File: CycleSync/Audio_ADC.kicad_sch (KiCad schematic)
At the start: 21 parts, among them U6 PCM1862DBT

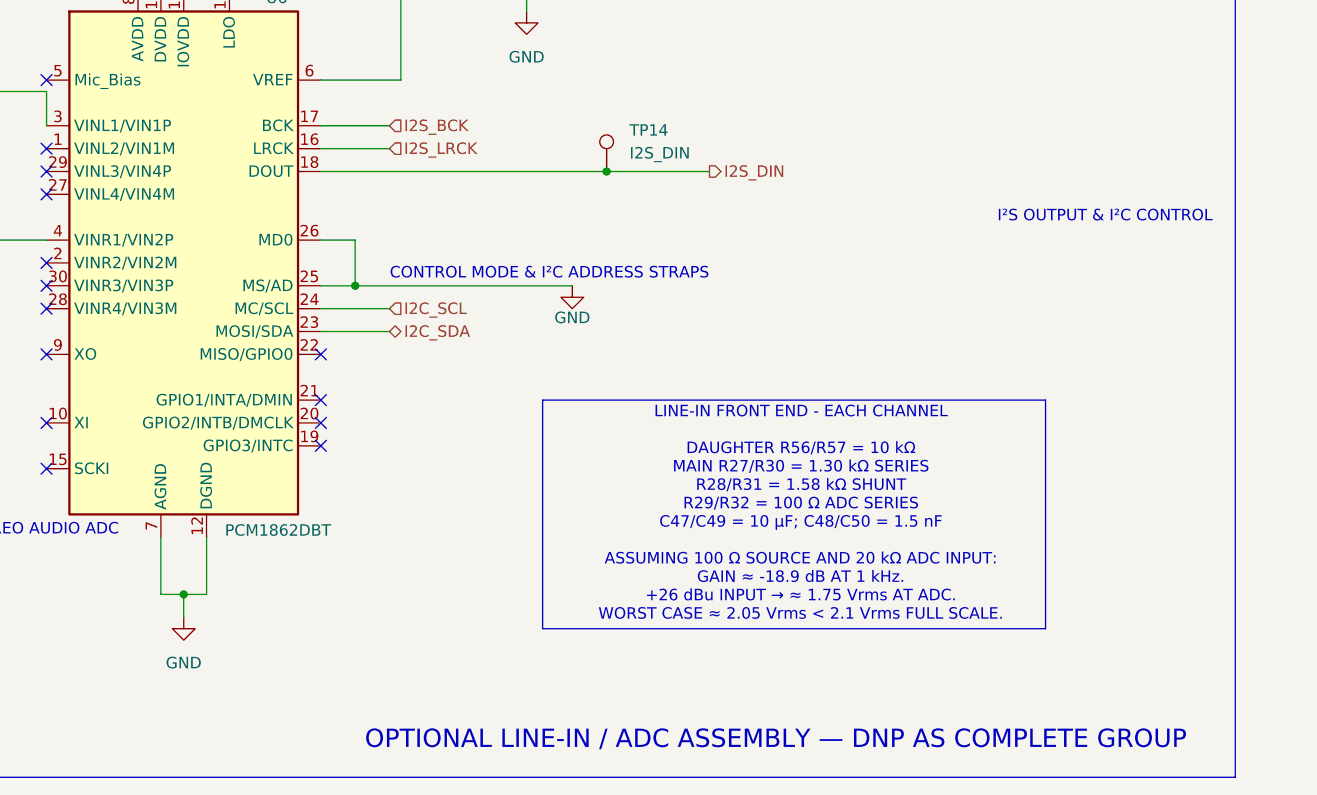
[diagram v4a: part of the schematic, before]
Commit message: added footprints and manufacturer part number
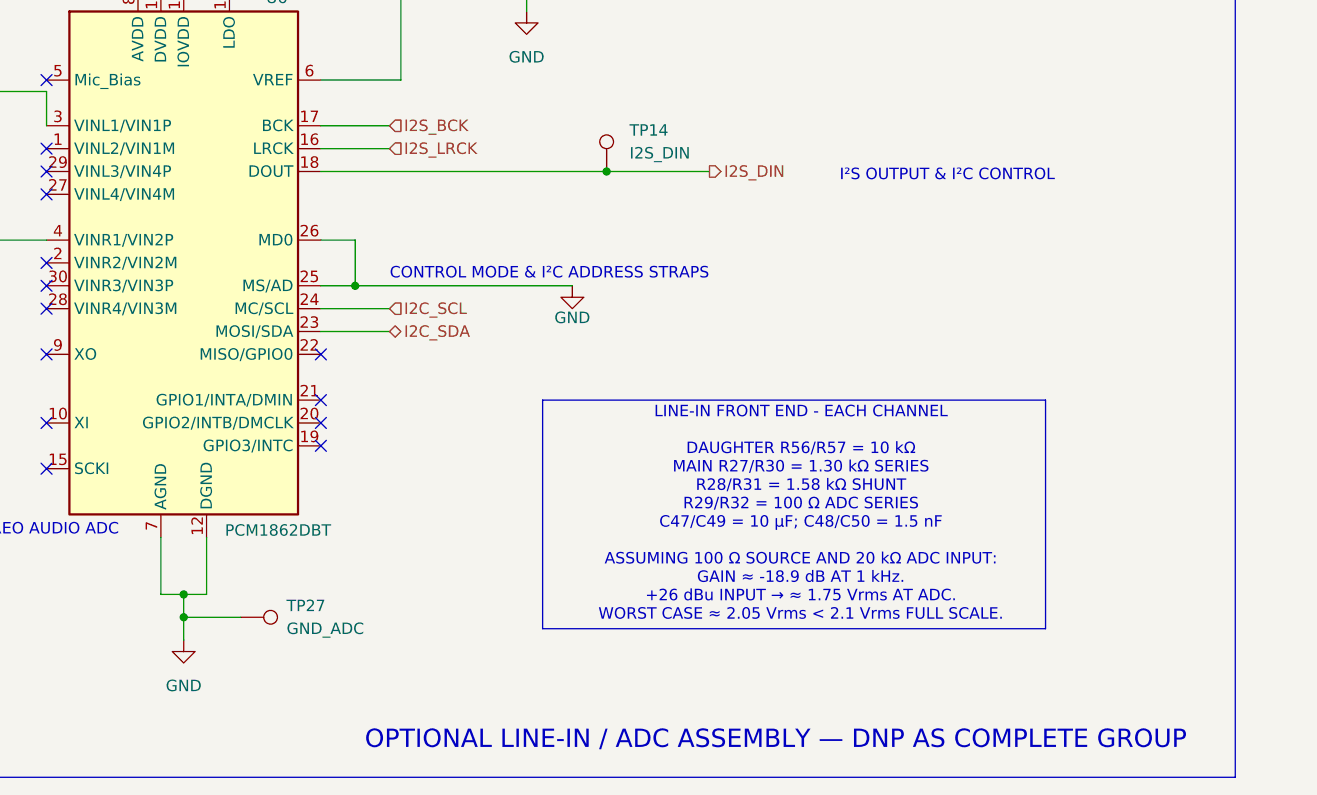
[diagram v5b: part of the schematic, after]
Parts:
- added TP27: GND_ADC, TestPoint:TestPoint_Pad_D1.5mm, symbol Connector:TestPoint
- C40, C42, C45: Distributor Link (none) -> https://jlcpcb.com/partdetail/MurataElectronics-GRM155R71A1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; MANUFACTURER (none) -> Murata Electronics; MPN (none) -> GRM155R71A104KA01D
- C41, C43, C46, C47, C49: Distributor Link (none) -> https://jlcpcb.com/partdetail/236937-GRM21BZ71E106KE15L/C23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; MANUFACTURER (none) -> Murata Electronics; MPN (none) -> GRM21BZ71E106KE15L
- C44: Distributor Link (none) -> https://jlcpcb.com/partdetail/30690-CL10B105KA8NNNC/C29936; MANUFACTURER (none) -> Samsung Electro-Mechanics; MPN (none) -> CL10B105KA8NNNC
- C48, C50: Distributor Link (none) -> https://jlcpcb.com/partdetail/173585-GRM1885C1H152JA01D/C16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; MANUFACTURER (none) -> Murata Electronics; MPN (none) -> GRM1885C1H152JA01D
- D4, D5: Distributor Link (none) -> https://jlcpcb.com/partdetail/Nexperia-PESD24VL1BA115/C69324; MANUFACTURER (none) -> Nexperia; MPN (none) -> PESD24VL1BA,115
- R27, R30: Distributor Link (none) -> https://jlcpcb.com/partdetail/23494-0603WAF1301T5E/C22767; MANUFACTURER (none) -> UNI-ROYAL(Uniroyal Elec); MPN (none) -> 0603WAF1301T5E
- R28, R31: Distributor Link (none) -> https://jlcpcb.com/partdetail/23495-0603WAF1581T5E/C22768; MANUFACTURER (none) -> UNI-ROYAL(Uniroyal Elec); MPN (none) -> 0603WAF1581T5E
- R29, R32: Distributor Link (none) -> https://jlcpcb.com/partdetail/23502-0603WAF1000T5E/C22775; MANUFACTURER (none) -> UNI-ROYAL(Uniroyal Elec); MPN (none) -> 0603WAF1000T5E
- TP14: now left out of the parts list
- U6: Distributor Link (none) -> https://jlcpcb.com/partdetail/TexasInstruments-PCM1862DBTR/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; MANUFACTURER (none) -> Texas Instruments; MPN (none) -> PCM1862DBTR
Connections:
- net GND: now also TP27.1
